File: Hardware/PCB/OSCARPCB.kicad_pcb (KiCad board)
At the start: 2 copper layers, 59.5 x 68 mm, 6 parts, among them J1 DC Motor, J2 Stepper Motor, J4 Servo OUT, J5 Power Input, J6 PINHD_1x2_Female, U2 ESP32-DevKitC

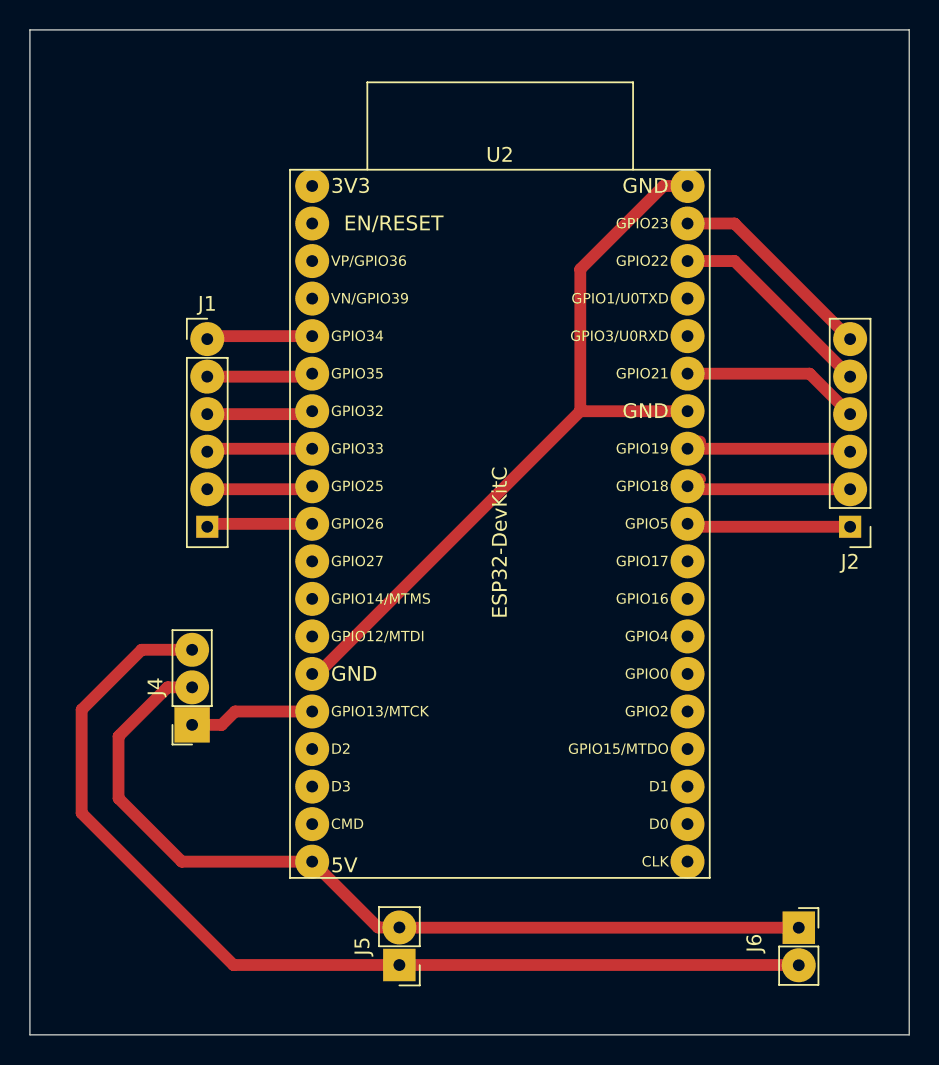
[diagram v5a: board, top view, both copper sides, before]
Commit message: Exported STEP file
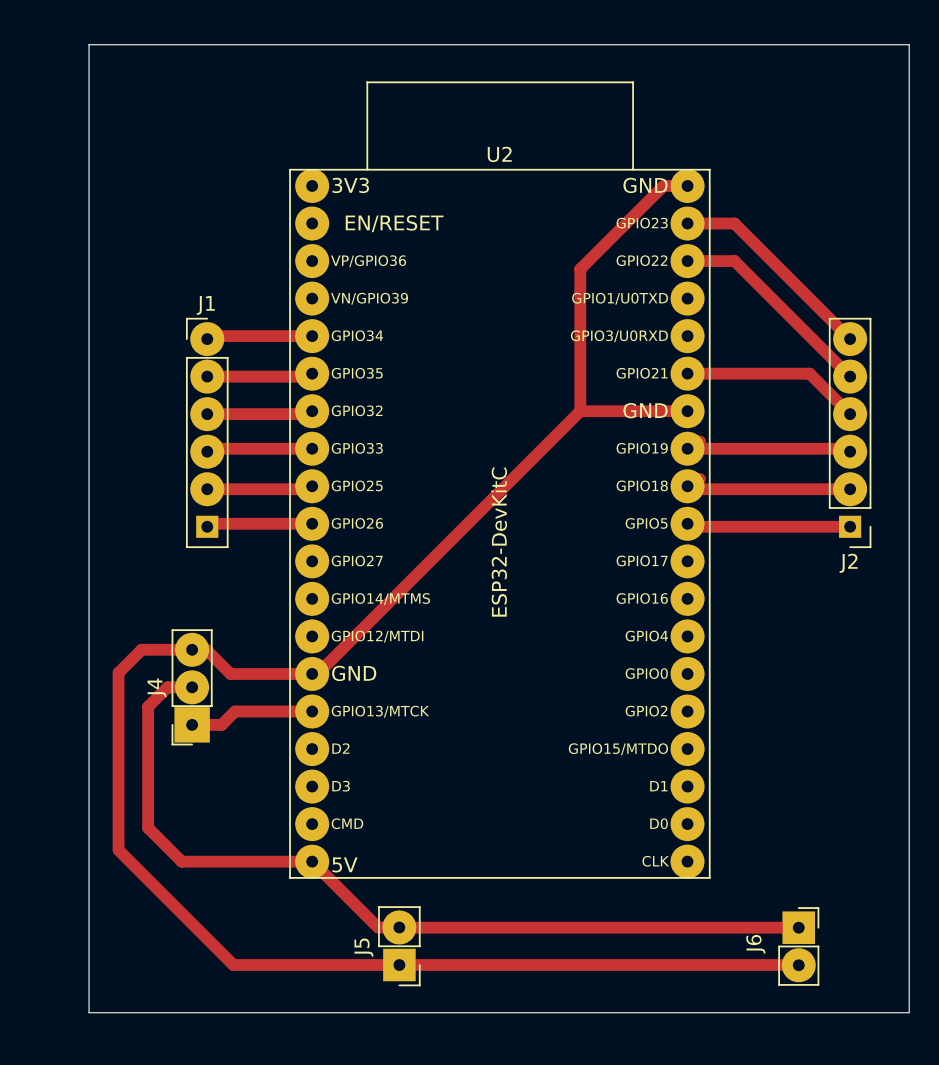
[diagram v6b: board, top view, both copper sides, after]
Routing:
- net GND: track 120.9 -> 127.6 mm
- net VBATT: track 60.2 -> 58.5 mm
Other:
- board size 59.5 x 68 mm -> 55.5 x 65.5 mm
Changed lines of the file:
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@@
 	)
 	(gr_rect
-		(start 84 75)
-		(end 143.5 143)
+		(start 88 76)
+		(end 143.5 141.5)
 		(stroke
 			(width 0.05)
@@
 		(fill no)
 		(layer "Edge.Cuts")
-	)
-	(segment
-		(start 91.555 116.945)
-		(end 94.975 116.945)
-		(width 0.8)
-		(layer "F.Cu")
-		(net 1)
-	)
-	(segment
-		(start 109 138.275)
-		(end 97.775 138.275)
-		(width 0.8)
-		(layer "F.Cu")
-		(net 1)
 	)
 	(segment
@@
 	)
 	(segment
-		(start 87.5 128)
-		(end 87.5 121)
+		(start 91.555 116.945)
+		(end 94.975 116.945)
 		(width 0.8)
 		(layer "F.Cu")
@@
 	)
 	(segment
-		(start 87.5 121)
-		(end 91.555 116.945)
-		(width 0.8)
-		(layer "F.Cu")
-		(net 1)
-	)
-	(segment
 		(start 136.01 138.275)
 		(end 136.025 138.29)
@@
 	)
 	(segment
-		(start 97.775 138.275)
-		(end 87.5 128)
+		(start 90 118.5)
+		(end 91.555 116.945)
 		(width 0.8)
 		(layer "F.Cu")
@@
 	)
 	(segment
+		(start 97.58 118.58)
+		(end 103.1 118.58)
+		(width 0.8)
+		(layer "F.Cu")
+		(net 1)
+	)
+	(segment
+		(start 97.775 138.275)
+		(end 90 130.5)
+		(width 0.8)
+		(layer "F.Cu")
+		(net 1)
+	)
+	(segment
+		(start 94.975 116.945)
+		(end 95.945 116.945)
+		(width 0.8)
+		(layer "F.Cu")
+		(net 1)
+	)
+	(segment
+		(start 95.945 116.945)
+		(end 97.58 118.58)
+		(width 0.8)
+		(layer "F.Cu")
+		(net 1)
+	)
+	(segment
 		(start 121.240553 100.8)
 		(end 103.460553 118.58)
+		(width 0.8)
+		(layer "F.Cu")
+		(net 1)
+	)
+	(segment
+		(start 90 130.5)
+		(end 90 118.5)
+		(width 0.8)
+		(layer "F.Cu")
+		(net 1)
+	)
+	(segment
+		(start 109 138.275)
+		(end 97.775 138.275)
 		(width 0.8)
 		(layer "F.Cu")
@@
 	)
 	(segment
+		(start 92 129)
+		(end 94.28 131.28)
+		(width 0.8)
+		(layer "F.Cu")
+		(net 2)
+	)
+	(segment
+		(start 93.313 119.485)
+		(end 92 120.798)
+		(width 0.8)
+		(layer "F.Cu")
+		(net 2)
+	)
+	(segment
 		(start 107.555 135.735)
 		(end 103.1 131.28)
@@
 	)
 	(segment
-		(start 90 122.798)
-		(end 90 127)
+		(start 94.28 131.28)
+		(end 103.1 131.28)
 		(width 0.8)
 		(layer "F.Cu")
@@
 	)
 	(segment
-		(start 93.313 119.485)
-		(end 90 122.798)
+		(start 109.015 135.75)
+		(end 109 135.735)
 		(width 0.8)
 		(layer "F.Cu")
@@
 		(start 94.975 119.485)
 		(end 93.313 119.485)
-		(width 0.8)
-		(layer "F.Cu")
-		(net 2)
-	)
-	(segment
-		(start 90 127)
-		(end 94.28 131.28)
-		(width 0.8)
-		(layer "F.Cu")
-		(net 2)
-	)
-	(segment
-		(start 109.015 135.75)
-		(end 109 135.735)
 		(width 0.8)
 		(layer "F.Cu")
@@
 	)
 	(segment
-		(start 94.28 131.28)
-		(end 103.1 131.28)
+		(start 92 120.798)
+		(end 92 129)
 		(width 0.8)
 		(layer "F.Cu")
